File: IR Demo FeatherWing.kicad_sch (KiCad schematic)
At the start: 32 parts, among them J1 Micro SD, J2 EXT A, J3 EXT B, U1 TFBS4711, U2 TFBS4711, U3 TFBS4711

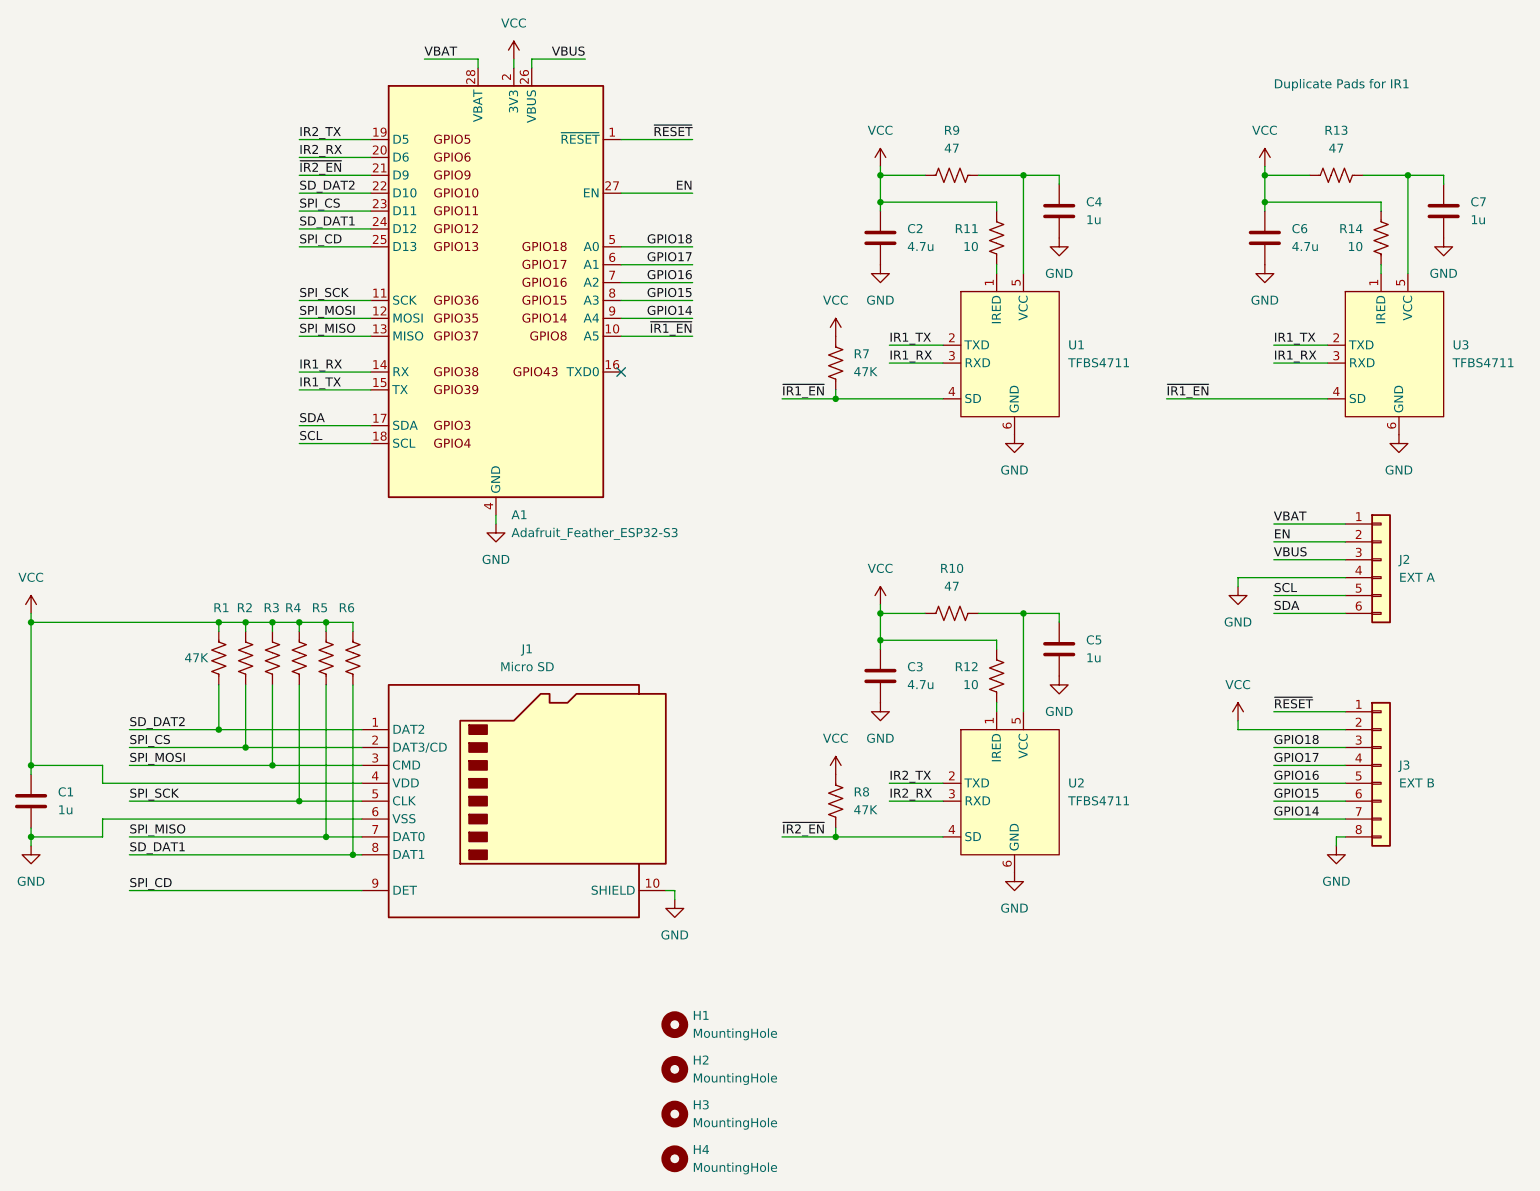
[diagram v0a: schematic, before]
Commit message: Add BOM and README
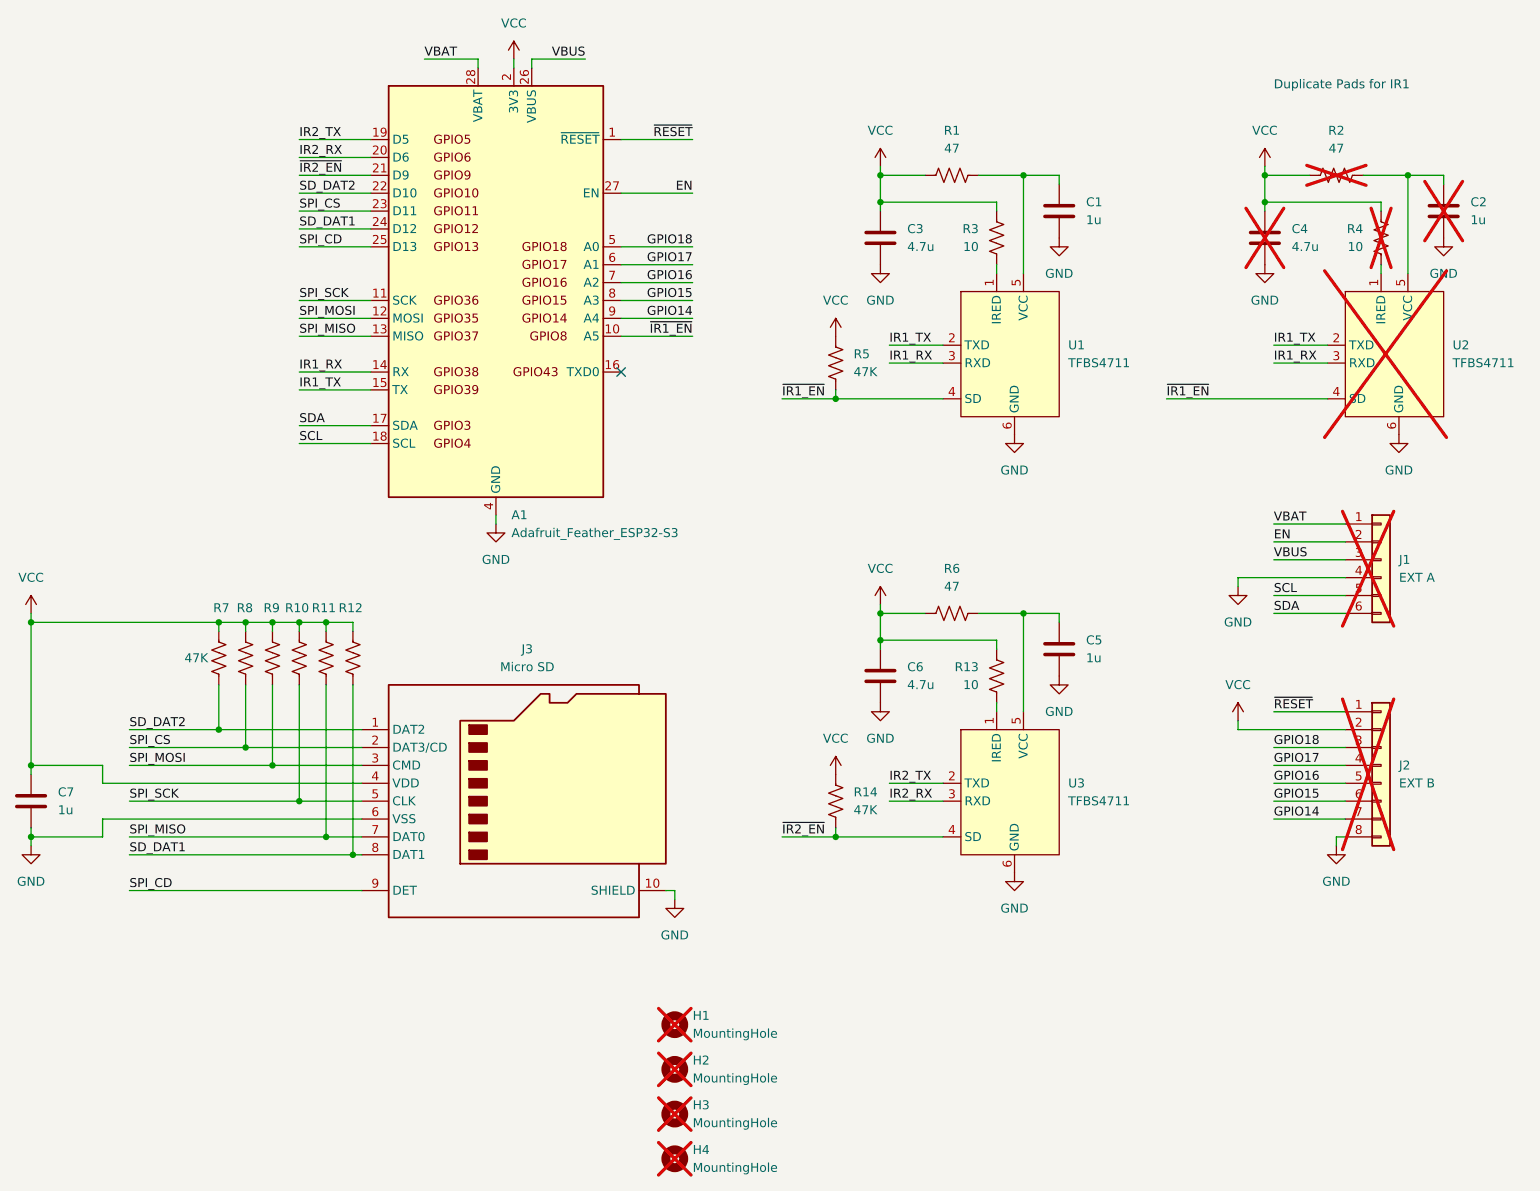
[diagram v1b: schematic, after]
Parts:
- A1: MPN (none) -> Adafruit 5477
- C1: renamed from C4; MPN (none) -> C0805C105Z4VACTU
- C2: renamed from C7; MPN (none) -> C0805C105Z4VACTU; now not fitted
- C3: renamed from C2; MPN (none) -> CL21A475KOFNNNE
- C4: renamed from C6; MPN (none) -> CL21A475KOFNNNE; now not fitted
- C5: MPN (none) -> C0805C105Z4VACTU
- C6: renamed from C3; MPN (none) -> CL21A475KOFNNNE
- C7: renamed from C1; MPN (none) -> C0805C105Z4VACTU
- H1, H2, H3, H4: MPN (none) -> -; now not fitted
- J1: renamed from J2; MPN (none) -> -; now not fitted
- J2: renamed from J3; MPN (none) -> -; now not fitted
- J3: renamed from J1; MPN (none) -> SameSky MSD-4-A
- R1: renamed from R9; MPN (none) -> WR08X470 JTL
- R10: renamed from R4; MPN (none) -> RMCF0805FT47K0
- R11: renamed from R5; MPN (none) -> RMCF0805FT47K0
- R12: renamed from R6; MPN (none) -> RMCF0805FT47K0
- R13: renamed from R12; MPN (none) -> WR08X100 JTL
- R14: renamed from R8; MPN (none) -> RMCF0805FT47K0
- R2: renamed from R13; MPN (none) -> WR08X470 JTL; now not fitted
- R3: renamed from R11; MPN (none) -> WR08X100 JTL
- R4: renamed from R14; MPN (none) -> WR08X100 JTL; now not fitted
- R5: renamed from R7; MPN (none) -> RMCF0805FT47K0
- R6: renamed from R10; MPN (none) -> WR08X470 JTL
- R7: renamed from R1; MPN (none) -> RMCF0805FT47K0
- R8: renamed from R2; MPN (none) -> RMCF0805FT47K0
- R9: renamed from R3; MPN (none) -> RMCF0805FT47K0
- U1: MPN (none) -> Vishay TFBS4711
- U2: renamed from U3; MPN (none) -> Vishay TFBS4711; now not fitted
- U3: renamed from U2; MPN (none) -> Vishay TFBS4711
